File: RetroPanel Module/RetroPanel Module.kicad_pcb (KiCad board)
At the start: 2 copper layers, 100 x 97.9 mm, 17 parts, among them J1 Front Panel, M1 Mounting_Pin, M10 Mounting_Pad, M11 Mounting_Pad, M12 Mounting_Pad, M13 Mounting_Pad, M14 Mounting_Pad, M15 Mounting_Pad, M16 Mounting_Pin, M2 Mounting_Pin, M3 Mounting_Pin, M4 Mounting_Pad, M5 Mounting_Pad, M6 Mounting_Pad, M7 Mounting_Pad, M8 Mounting_Pad, M9 Mounting_Pad

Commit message: First schematic draft
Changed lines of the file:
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@@
     (descr "Alps rotary encoder, EC12E... with switch, vertical shaft, http://www.alps.com/prod/info/E/HTML/Encoder/Incremental/EC11/EC11E15204A3.html")
     (tags "rotary encoder")
-    (fp_text reference J1 (at 5.979 2.3368 90) (layer F.SilkS)
-      (effects (font (size 1 1) (thickness 0.15)))
-    )
-    (fp_text value "Front Panel" (at 0 2.3368 270) (layer F.SilkS)
-      (effects (font (size 1 1) (thickness 0.15)))
-    )
+    (fp_text reference J1 (at -6.086 2.3368 270 unlocked) (layer F.SilkS)
+      (effects (font (size 1 1) (thickness 0.15)))
+    )
+    (fp_text value "Front Panel" (at 0 2.3368 270 unlocked) (layer F.SilkS)
+      (effects (font (size 1 1) (thickness 0.15)))
+    )
+    (fp_line (start 0 3.048) (end 0 4.826) (layer F.SilkS) (width 0.05))
+    (fp_line (start 2.523 15.804) (end 2.523 5.804) (layer Dwgs.User) (width 0.05))
+    (fp_line (start -2.777 15.804) (end -2.777 5.804) (layer Dwgs.User) (width 0.05))
+    (fp_line (start -2.777 15.804) (end 2.523 15.804) (layer Dwgs.User) (width 0.05))
+    (fp_line (start -48.95 3.937) (end 48.95 3.937) (layer F.SilkS) (width 0.05))
+    (fp_line (start -48.95 5.715) (end 48.95 5.715) (layer F.SilkS) (width 0.05))
+    (fp_line (start 48.95 3.937) (end 48.95 5.715) (layer F.SilkS) (width 0.05))
+    (fp_line (start -48.95 3.937) (end -48.95 5.715) (layer F.SilkS) (width 0.05))
+    (fp_line (start -28.3 3.937) (end -28.3 5.715) (layer F.SilkS) (width 0.05))
+    (fp_line (start -22.5 3.937) (end -22.5 5.715) (layer F.SilkS) (width 0.05))
+    (fp_line (start 22.5 5.715) (end 22.5 3.937) (layer F.SilkS) (width 0.05))
     (fp_line (start 28.3 5.715) (end 28.3 3.937) (layer F.SilkS) (width 0.05))
-    (fp_line (start 22.5 5.715) (end 22.5 3.937) (layer F.SilkS) (width 0.05))
-    (fp_line (start -22.5 3.937) (end -22.5 5.715) (layer F.SilkS) (width 0.05))
-    (fp_line (start -28.3 3.937) (end -28.3 5.715) (layer F.SilkS) (width 0.05))
-    (fp_line (start -48.95 3.937) (end -48.95 5.715) (layer F.SilkS) (width 0.05))
-    (fp_line (start 48.95 3.937) (end 48.95 5.715) (layer F.SilkS) (width 0.05))
-    (fp_line (start -48.95 5.715) (end 48.95 5.715) (layer F.SilkS) (width 0.05))
-    (fp_line (start -48.95 3.937) (end 48.95 3.937) (layer F.SilkS) (width 0.05))
-    (fp_line (start -2.777 15.804) (end 2.523 15.804) (layer Dwgs.User) (width 0.05))
-    (fp_line (start -2.777 15.804) (end -2.777 5.804) (layer Dwgs.User) (width 0.05))
-    (fp_line (start 2.523 15.804) (end 2.523 5.804) (layer Dwgs.User) (width 0.05))
-    (fp_line (start 0 3.048) (end 0 4.826) (layer F.SilkS) (width 0.05))
     (pad 26 thru_hole circle (at 31.75 0 270) (size 1.524 1.524) (drill 0.762) (layers *.Cu *.Mask)
       (net 1 GND))
@@
       (effects (font (size 1 1) (thickness 0.15)))
     )
-    (fp_circle (center 0 0) (end 2 0.8) (layer F.Fab) (width 0.1))
-    (fp_circle (center 0 0) (end 2.6 0) (layer F.CrtYd) (width 0.05))
+    (fp_circle (center 0 0) (end 2.6 0) (layer F.CrtYd) (width 0.05))
+    (fp_circle (center 0 0) (end 2 0.8) (layer F.Fab) (width 0.1))
     (pad 1 thru_hole circle (at 0 0) (size 3.5 3.5) (drill 3.048) (layers *.Cu *.Mask)
       (net 1 GND) (solder_mask_margin 0.8))
@@
       (effects (font (size 1 1) (thickness 0.15)))
     )
-    (fp_circle (center 0 0) (end 2.6 0) (layer F.CrtYd) (width 0.05))
-    (fp_circle (center 0 0) (end 2 0.8) (layer F.Fab) (width 0.1))
+    (fp_circle (center 0 0) (end 2 0.8) (layer F.Fab) (width 0.1))
+    (fp_circle (center 0 0) (end 2.6 0) (layer F.CrtYd) (width 0.05))
     (pad 1 thru_hole circle (at 0 0) (size 3.5 3.5) (drill 3.048) (layers *.Cu *.Mask)
       (net 1 GND) (solder_mask_margin 0.8))
@@
       (effects (font (size 1 1) (thickness 0.15)))
     )
-    (fp_circle (center 0 0) (end 2 0.8) (layer F.Fab) (width 0.1))
-    (fp_circle (center 0 0) (end 2.6 0) (layer F.CrtYd) (width 0.05))
+    (fp_circle (center 0 0) (end 2.6 0) (layer F.CrtYd) (width 0.05))
+    (fp_circle (center 0 0) (end 2 0.8) (layer F.Fab) (width 0.1))
     (pad 1 thru_hole circle (at 0 0) (size 3.5 3.5) (drill 3.048) (layers *.Cu *.Mask)
       (net 1 GND) (solder_mask_margin 0.8))
@@
       (effects (font (size 1 1) (thickness 0.15)))
     )
-    (fp_circle (center 0 0) (end 2 0.8) (layer F.Fab) (width 0.1))
-    (fp_circle (center 0 0) (end 2.6 0) (layer F.CrtYd) (width 0.05))
-    (pad 1 thru_hole circle (at 0 0) (size 3.5 3.5) (drill 3.048) (layers *.Cu *.Mask)
-      (net 1 GND) (solder_mask_margin 0.8))
+    (fp_circle (center 0 0) (end 2.6 0) (layer F.CrtYd) (width 0.05))
+    (fp_circle (center 0 0) (end 2 0.8) (layer F.Fab) (width 0.1))
+    (pad 1 thru_hole circle (at 0 0) (size 3.5 3.5) (drill 3.048) (layers *.Cu *.Mask)
+      (net 1 GND) (solder_mask_margin 0.8))

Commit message: First layout draft done
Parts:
- added A1: Arduino_Pro_Micro, arduino_pro_micro:Arduino_Pro_Micro, F.Cu at (183.6, 70.1)
- added C1: 1uF, RetroPanel:CP_Radial_D4.0mm_P2.00mm_Custom, F.Cu at (131.6, 75.9)
- added C2: 1uF, RetroPanel:CP_Radial_D4.0mm_P2.00mm_Custom, F.Cu at (147.4, 75.9)
- added C3: 1uF, RetroPanel:CP_Radial_D4.0mm_P2.00mm_Custom, F.Cu at (134.8, 75.9)
- added C4: 1uF, RetroPanel:CP_Radial_D4.0mm_P2.00mm_Custom, F.Cu at (125.2, 69.6)
- added C5: 100nF, Capacitor_THT:C_Disc_D4.7mm_W2.5mm_P5.00mm, F.Cu at (129.7, 60.0)
- added C6: 100nF, Capacitor_THT:C_Disc_D4.7mm_W2.5mm_P5.00mm, F.Cu at (172.2, 130.5)
- added C7: 4.7uF, RetroPanel:CP_Radial_D4.0mm_P2.00mm_Custom, F.Cu at (167.1, 141.3)
- added C8: 1000nF, Capacitor_THT:C_Disc_D4.7mm_W2.5mm_P5.00mm, F.Cu at (190.0, 139.4)
- added D1: 1N4001, Diode_THT:D_DO-41_SOD81_P10.16mm_Horizontal, F.Cu at (168.4, 58.1)
- added J10: SW_EXTRA, RetroPanel:PinHeader_1x02_P2.54mm_Vertical, F.Cu at (179.8, 124.1)
- added J11: RS-232, Connector_IDC:IDC-Header_2x05_P2.54mm_Vertical, F.Cu at (160.1, 75.2)
- added J12: +5VSB, RetroPanel:PSU_Wire, F.Cu at (197.0, 130.5)
- added J13: PWR_ON, RetroPanel:PSU_Wire, F.Cu at (198.2, 134.9)
- added J14: PWR_OK, RetroPanel:PSU_Wire, F.Cu at (197.0, 139.4)
- added J15: COMMON, RetroPanel:PSU_Wire, F.Cu at (198.2, 143.8)
- added J16: SPEAKER, RetroPanel:PinHeader_1x04_P2.54mm_Vertical, F.Cu at (173.5, 112.1)
- added J2: SW_POWER, RetroPanel:PinHeader_1x02_P2.54mm_Vertical, F.Cu at (186.8, 92.1)
- added J3: LED_POWER, RetroPanel:PinHeader_1x02_P2.54mm_Vertical, F.Cu at (186.8, 85.4)
- added J4: SW_RESET, RetroPanel:PinHeader_1x02_P2.54mm_Vertical, F.Cu at (186.8, 98.7)
- added J5: SW_TURBO, RetroPanel:PinHeader_1x02_P2.54mm_Vertical, F.Cu at (186.8, 105.1)
- added J6: LED_TURBO, RetroPanel:PinHeader_1x02_P2.54mm_Vertical, F.Cu at (186.8, 112.1)
- added J7: POWER, RetroPanel:Molex_KK-254_1x04_P2.54mm_Horizontal, F.Cu at (187.4, 126.7)
- added J8: IIC, Connector_PinHeader_2.54mm:PinHeader_1x04_P2.54mm_Vertical, F.Cu at (177.3, 54.3)
- added J9: POST_CARD, Connector_IDC:IDC-Header_2x10_P2.54mm_Vertical, F.Cu at (197.6, 110.1)
- added JP1: LED_PWR1, solder_bridge:select, F.Cu at (143.6, 91.7)
- added JP2: LED_PWR2, solder_bridge:select, F.Cu at (148.7, 91.7)
- added JP3: TURBO_SEL, solder_bridge:select, F.Cu at (176.0, 98.7)
- added JP4: LED_VCC, solder_bridge:select, F.Cu at (153.8, 91.7)
- added JP5: 7S_TYPE, solder_bridge:select, F.Cu at (125.8, 106.3)
- added LS1: Speaker, Buzzer_Beeper:Buzzer_12x9.5RM7.6, F.Cu at (135.4, 136.8)
- added Q1: 2N3904, Package_TO_SOT_THT:TO-92_Inline_Wide, F.Cu at (129.0, 108.2)
- added Q2: 2N3904, Package_TO_SOT_THT:TO-92_Inline_Wide, F.Cu at (129.0, 113.3)
- added Q3: 2N3904, Package_TO_SOT_THT:TO-92_Inline_Wide, F.Cu at (129.0, 118.4)
- added Q4: 2N3904, Package_TO_SOT_THT:TO-92_Inline_Wide, F.Cu at (129.0, 123.5)
- added R1: 4k7, resistor:R_Axial_DIN0207_L6.3mm_D2.5mm_P10.16mm_Horizontal, F.Cu at (155.1, 57.4)
- added R10: 470, resistor:R_Axial_DIN0207_L6.3mm_D2.5mm_P10.16mm_Horizontal, F.Cu at (167.1, 95.5)
- added R11: 470, resistor:R_Axial_DIN0207_L6.3mm_D2.5mm_P10.16mm_Horizontal, F.Cu at (163.9, 95.5)
- added R12: 470, resistor:R_Axial_DIN0207_L6.3mm_D2.5mm_P10.16mm_Horizontal, F.Cu at (160.8, 95.5)
- added R13: 10k, resistor:R_Axial_DIN0207_L6.3mm_D2.5mm_P10.16mm_Horizontal, F.Cu at (138.6, 90.5)
- added R14: 10k, resistor:R_Axial_DIN0207_L6.3mm_D2.5mm_P10.16mm_Horizontal, F.Cu at (138.6, 87.3)
- added R15: 10k, resistor:R_Axial_DIN0207_L6.3mm_D2.5mm_P10.16mm_Horizontal, F.Cu at (138.6, 84.1)
- added R16: 10k, resistor:R_Axial_DIN0207_L6.3mm_D2.5mm_P10.16mm_Horizontal, F.Cu at (138.6, 80.9)
- added R17: 0, resistor:R_Axial_DIN0207_L6.3mm_D2.5mm_P10.16mm_Horizontal, F.Cu at (143.6, 85.4)
- added R18: 33k, resistor:R_Axial_DIN0207_L6.3mm_D2.5mm_P10.16mm_Horizontal, F.Cu at (179.8, 130.5)
- added R19: 27k, resistor:R_Axial_DIN0207_L6.3mm_D2.5mm_P10.16mm_Horizontal, F.Cu at (193.2, 134.9)
- added R2: 4k7, resistor:R_Axial_DIN0207_L6.3mm_D2.5mm_P10.16mm_Horizontal, F.Cu at (165.2, 54.3)
- added R20: 220k, resistor:R_Axial_DIN0207_L6.3mm_D2.5mm_P10.16mm_Horizontal, F.Cu at (167.1, 147.0)
- added R3: 0, resistor:R_Axial_DIN0207_L6.3mm_D2.5mm_P10.16mm_Horizontal, F.Cu at (179.8, 112.1)
- added R4: 470, resistor:R_Axial_DIN0207_L6.3mm_D2.5mm_P10.16mm_Horizontal, F.Cu at (153.8, 99.4)
- added R5: 470, resistor:R_Axial_DIN0207_L6.3mm_D2.5mm_P10.16mm_Horizontal, F.Cu at (157.6, 95.5)
- added R6: 470, resistor:R_Axial_DIN0207_L6.3mm_D2.5mm_P10.16mm_Horizontal, F.Cu at (179.8, 95.5)
- added R7: 470, resistor:R_Axial_DIN0207_L6.3mm_D2.5mm_P10.16mm_Horizontal, F.Cu at (176.7, 95.5)
- added R8: 470, resistor:R_Axial_DIN0207_L6.3mm_D2.5mm_P10.16mm_Horizontal, F.Cu at (173.5, 95.5)
- added R9: 470, resistor:R_Axial_DIN0207_L6.3mm_D2.5mm_P10.16mm_Horizontal, F.Cu at (170.3, 95.5)
- added U1: MAX232, Package_DIP:DIP-16_W7.62mm_Socket_LongPads, F.Cu at (129.7, 71.4)
- added U2: NE555P, Package_DIP:DIP-8_W7.62mm_Socket_LongPads, F.Cu at (172.2, 142.5)
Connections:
- J1 pad 1: (no net) -> +5V
- J1 pad 10: (no net) -> /7S_F
- J1 pad 11: (no net) -> /7S_E
- J1 pad 12: (no net) -> /7S_D
- J1 pad 13: (no net) -> /7S_DP
- J1 pad 14: (no net) -> /7S_C
- J1 pad 15: (no net) -> /7S_G
- J1 pad 16: (no net) -> /7S_D4
- J1 pad 17: (no net) -> /7S_D2
- J1 pad 18: (no net) -> /7S_D3
- J1 pad 19: (no net) -> /7S_B
- J1 pad 2: (no net) -> SW_PWR1
- J1 pad 20: (no net) -> SW_EXTRA1
- J1 pad 21: (no net) -> SW_EXTRA2
- J1 pad 22: (no net) -> SW_TURBO1
- J1 pad 23: (no net) -> SW_TURBO2
- J1 pad 24: (no net) -> LED_TURBO1
- J1 pad 25: (no net) -> LED_TURBO2
- J1 pad 3: (no net) -> SW_PWR2
- J1 pad 4: (no net) -> LED_PWR1
- J1 pad 5: (no net) -> LED_PWR2
- J1 pad 6: (no net) -> SW_RESET1
- J1 pad 7: (no net) -> SW_RESET2
- J1 pad 8: (no net) -> /7S_D1
- J1 pad 9: (no net) -> /7S_A
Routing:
- net +5V: track 0.00 -> 303.0 mm, vias 0 -> 3
- net SW_PWR1: track 0.00 -> 177.7 mm, vias 0 -> 2
- net SW_PWR2: track 0.00 -> 177.0 mm, vias 0 -> 1
- net SW_EXTRA1: track 0.00 -> 139.7 mm
- net SW_EXTRA2: track 0.00 -> 136.3 mm
- net /7S_A: track 0.00 -> 119.7 mm, vias 0 -> 4
- net /7S_D1: track 0.00 -> 116.7 mm
- net /7S_B: track 0.00 -> 115.0 mm, vias 0 -> 3
- net /7S_E: track 0.00 -> 111.5 mm, vias 0 -> 2
- net /7S_F: track 0.00 -> 109.5 mm, vias 0 -> 2
- net SW_TURBO1: track 0.00 -> 108.6 mm, vias 0 -> 1
- net /7S_G: track 0.00 -> 102.9 mm
- net /7S_D: track 0.00 -> 102.2 mm, vias 0 -> 4
- net /7S_C: track 0.00 -> 100.2 mm, vias 0 -> 4
- net /7S_D4: track 0.00 -> 98.6 mm, vias 0 -> 1
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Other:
- outline, holes or cut-outs redrawn
- board text added: "4x 2N3904"
- board text added: "7 segment type (JP5): CK: CA:"
- board text added: "JP1 (1-2), JP2 (1-2) JP1 (2-3), JP2 (2-3), JP4 (2-3) JP1 (2-3), JP2 (2-3), JP4 (1-2)"
- board text added: "JP3 (1-2) JP3 (2-3)"
- board text added: "JP5 (1-2) JP5 (2-3) reverse Q1-Q4"
- board text added: "Power LED: From MB: Direct VCC: Arduino:"
- board text added: "Turbo SEL: Switch (Pin 1): Sense LED:"

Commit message: Small tweaks
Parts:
- added G***: LOGO, RetroPanel:logo, F.Cu at (156.6, 125.1)
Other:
- board text added: "+5V"
- board text added: "3.5" RetroPanel Module (rev. A) github.com/tebl"
- board text added: "GND"
- board text removed: "RetroPanel Module (rev. A) github.com/tebl"

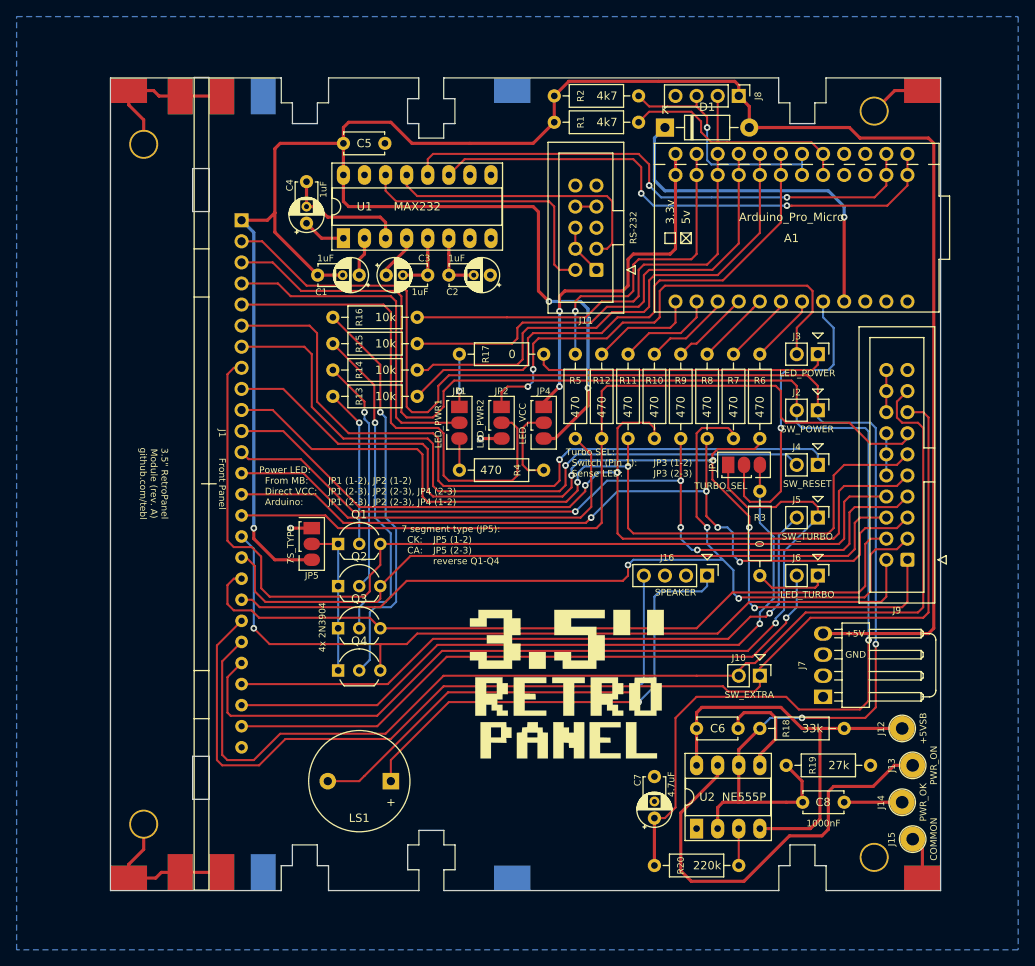
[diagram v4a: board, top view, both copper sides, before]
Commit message: Faceplate FP1 and HDD LED
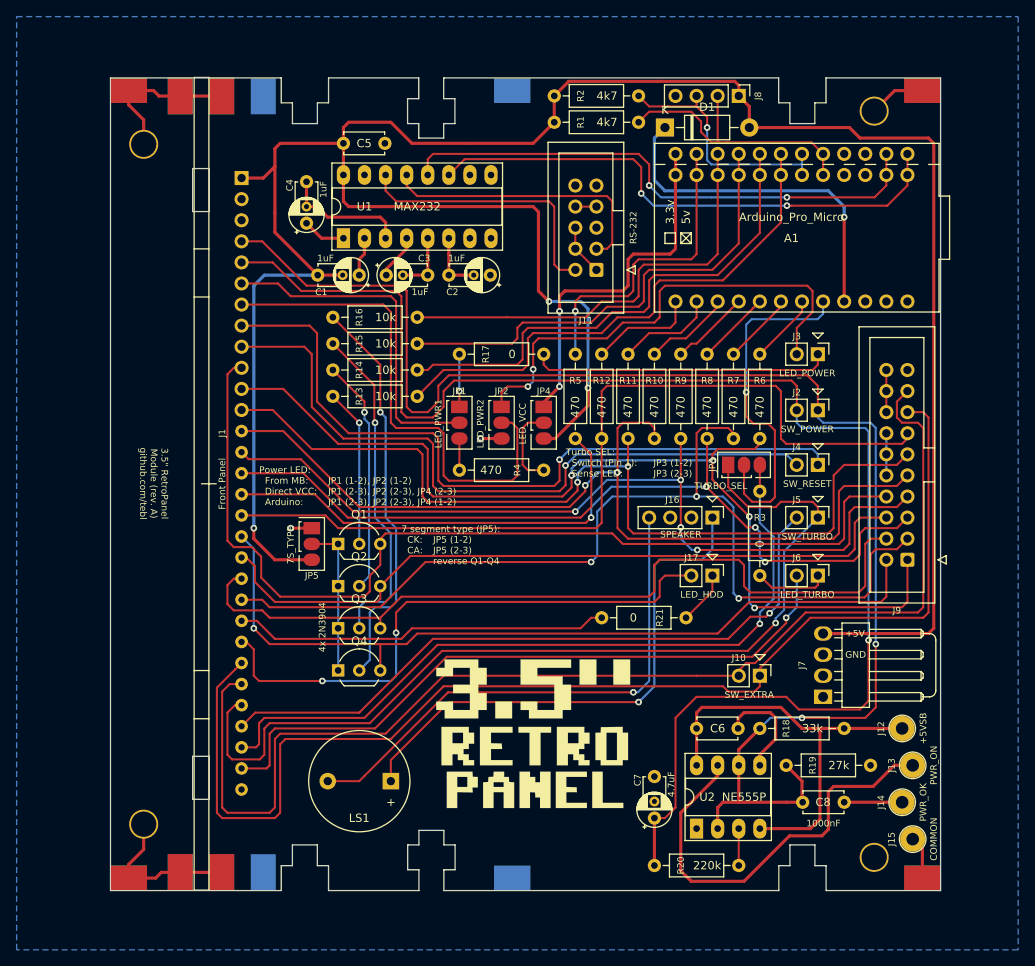
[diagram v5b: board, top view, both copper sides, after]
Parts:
- added J17: LED_HDD, RetroPanel:PinHeader_1x02_P2.54mm_Vertical, F.Cu at (174.1, 112.1)
- added R21: 0, resistor:R_Axial_DIN0207_L6.3mm_D2.5mm_P10.16mm_Horizontal, F.Cu at (170.9, 117.1)
- moved G*** 7.22 mm to (152.5, 131.1)
- moved J16 7.01 mm to (174.1, 105.1)
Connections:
- J1 pad 10: /7S_F -> /7S_D1
- J1 pad 11: /7S_E -> /7S_A
- J1 pad 12: /7S_D -> /7S_F
- J1 pad 13: /7S_DP -> /7S_E
- J1 pad 14: /7S_C -> /7S_D
- J1 pad 15: /7S_G -> /7S_DP
- J1 pad 16: /7S_D4 -> /7S_C
- J1 pad 17: /7S_D2 -> /7S_G
- J1 pad 18: /7S_D3 -> /7S_D4
- J1 pad 19: /7S_B -> /7S_D2
- J1 pad 2: SW_PWR1 -> (no net)
- J1 pad 20: SW_EXTRA1 -> /7S_D3
- J1 pad 21: SW_EXTRA2 -> /7S_B
- J1 pad 22: SW_TURBO1 -> LED_HDD1
- J1 pad 23: SW_TURBO2 -> LED_HDD2
- J1 pad 24: LED_TURBO1 -> SW_EXTRA1
- J1 pad 25: LED_TURBO2 -> SW_EXTRA2
- J1 pad 26: GND -> SW_TURBO1
- J1 pad 3: SW_PWR2 -> (no net)
- J1 pad 4: LED_PWR1 -> SW_PWR1
- J1 pad 5: LED_PWR2 -> SW_PWR2
- J1 pad 6: SW_RESET1 -> LED_PWR1
- J1 pad 7: SW_RESET2 -> LED_PWR2
- J1 pad 8: /7S_D1 -> SW_RESET1
- J1 pad 9: /7S_A -> SW_RESET2
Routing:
- net LED_HDD2: track 0.00 -> 68.8 mm, vias 0 -> 2
- net LED_HDD1: track 0.00 -> 45.3 mm
- net SW_EXTRA2: track 136.3 -> 145.9 mm
- net SW_EXTRA1: track 139.7 -> 148.4 mm
- net Net-(J16-Pad4): track 55.8 -> 63.4 mm
- net Net-(J16-Pad1): track 56.9 -> 64.2 mm
- net /7S_D3: track 92.3 -> 99.2 mm
- net Net-(J17-Pad1): track 0.00 -> 6.40 mm
- net SW_TURBO1: track 108.6 -> 113.2 mm
- net Net-(A1-Pad20): track 38.0 -> 42.4 mm
- net LED_TURBO2: track 77.0 -> 81.3 mm
- net /7S_B: track 115.0 -> 119.2 mm
- net LED_TURBO1: track 87.0 -> 90.6 mm
- net SW_TURBO2: track 80.0 -> 82.1 mm
- net /7S_G: track 102.9 -> 104.4 mm
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
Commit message: Export files
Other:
- board text added: "JLCJLCJLCJLC"

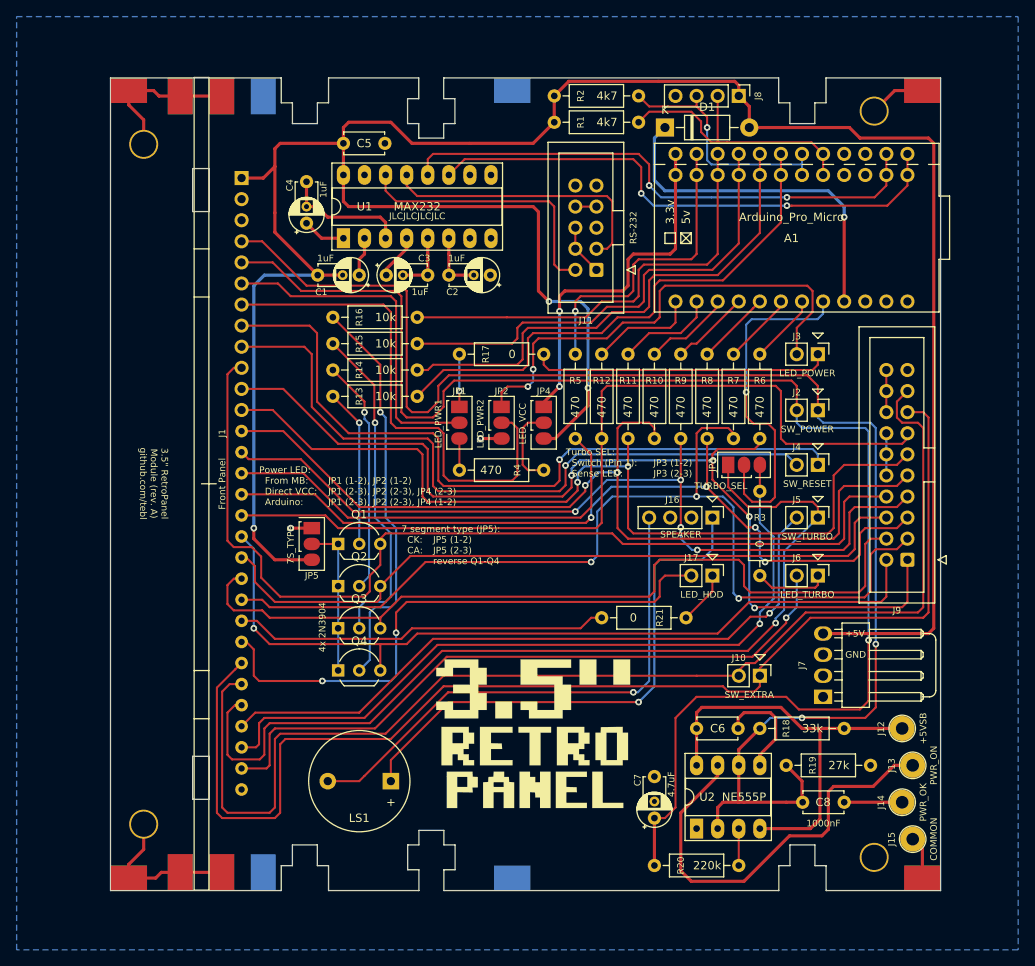
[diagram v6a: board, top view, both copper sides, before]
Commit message: Moved power diode
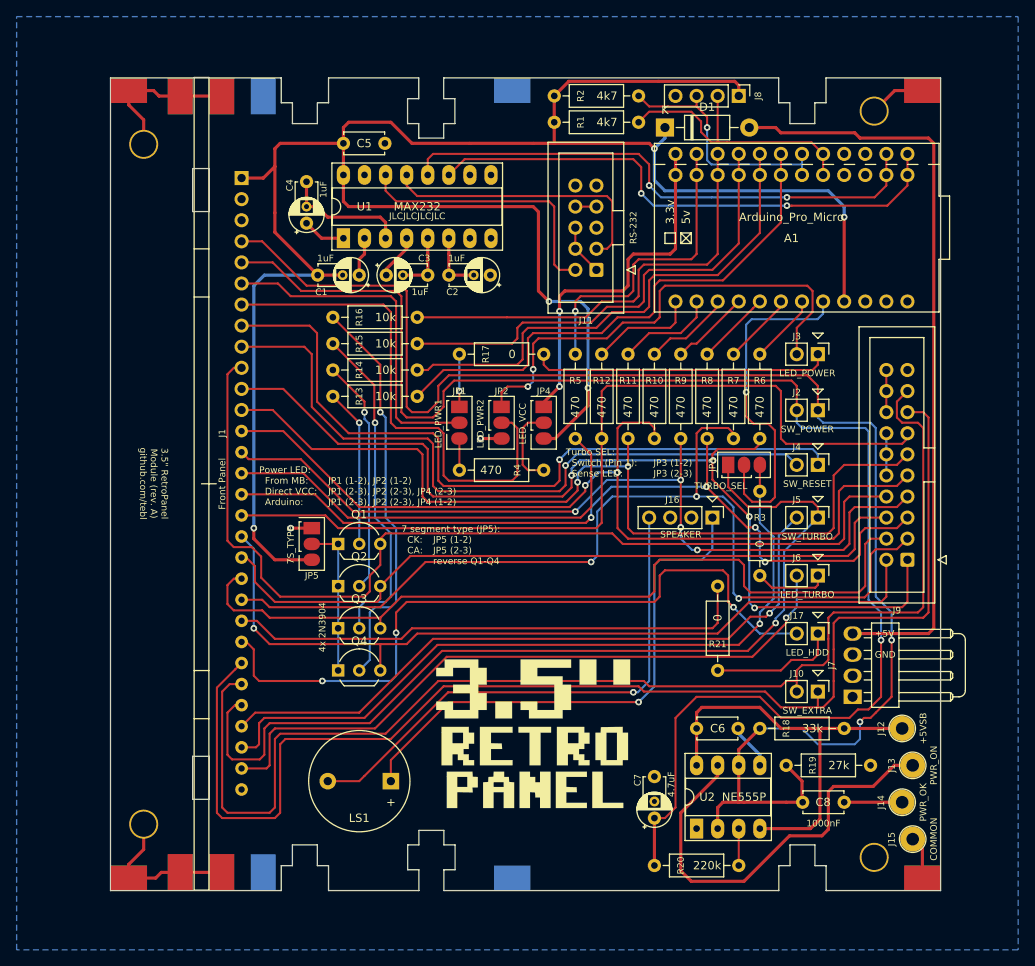
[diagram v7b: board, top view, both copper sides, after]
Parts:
- moved J17 14.5 mm to (186.8, 119.0)
- moved R21 7.41 mm to (174.7, 123.5), turned to 90 degrees
- moved J10 7.24 mm to (186.8, 126.0)
- moved J7 3.56 mm to (191.0, 126.7)
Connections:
- A1 pad 21: Net-(A1-Pad21) -> +5V
- D1 pad 1: Net-(A1-Pad21) -> +5V
- D1 pad 2: +5V -> Net-(D1-Pad2)
- J7 pad 4: +5V -> Net-(D1-Pad2)
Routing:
- net Net-(D1-Pad2): track 0.00 -> 92.1 mm
- net +5V: track 302.9 -> 259.8 mm, vias 3 -> 5
- net Net-(A1-Pad21): track 42.5 -> 0.00 mm, vias 1 -> 0
- net LED_HDD2: track 68.8 -> 87.2 mm, vias 2 -> 3
- net LED_HDD1: track 45.3 -> 63.5 mm
- net Net-(J17-Pad1): track 6.40 -> 15.4 mm
- net SW_EXTRA1: track 148.4 -> 155.9 mm
- net Net-(C6-Pad2): track 12.8 -> 5.53 mm
- net SW_EXTRA2: track 145.9 -> 151.0 mm
- net SW_PWR1: track 177.7 -> 182.5 mm
- net SW_PWR2: track 177.0 -> 179.7 mm

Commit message: Small tweaks
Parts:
- C7: footprint RetroPanel:CP_Radial_D4.0mm_P2.00mm_Custom -> Capacitor_THT:CP_Radial_D4.0mm_P2.00mm
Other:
- board text added: "LED_HDD"
- board text added: "LED_PWR"
- board text added: "LED_TURBO"
